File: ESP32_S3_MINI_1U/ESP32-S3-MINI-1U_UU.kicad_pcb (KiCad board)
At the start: 2 copper layers, 20.3 x 38.1 mm, 39 parts, among them IC1 TPS6282533DMQR, J1 Castellated_1x07, J2 USB4120-03-C, J3 Qwiic_Vertical, J4 Castellated_1x01, J5 Castellated_1x13, J6 Castellated_1x15, U1 ESP32-S3-MINI-1U, U2 LM66100DCK, U3 LM66100DCK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

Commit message: Sync Update
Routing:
- net IO3: track 6.08 -> 7.15 mm
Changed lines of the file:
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@@
-	)
-	(segment
-		(start 179.2 131.04)
-		(end 178.788768 130.628768)
-		(width 0.15)
-		(layer "F.Cu")
-		(net 7)
 	)
 	(segment
@@
 	)
 	(via
-		(at 178.76 130.7)
+		(at 179.2 131.04)
 		(size 0.5)
 		(drill 0.3)
@@
 	)
 	(segment
-		(start 178.831232 130.628768)
-		(end 178.76 130.557536)
+		(start 179.2 131.04)
+		(end 179.2 129.736388)
 		(width 0.15)
 		(layer "B.Cu")
@@
 	)
 	(segment
+		(start 179.2 129.736388)
+		(end 178.209 128.745388)
+		(width 0.15)
+		(layer "B.Cu")
+		(net 7)
+	)
+	(segment
 		(start 178.209 121.359)
-		(end 178.209 128.745388)
+		(end 175.95 119.1)
 		(width 0.15)
 		(layer "B.Cu")
@@
 	(segment
 		(start 178.209 128.745388)
-		(end 178.76 129.296388)
+		(end 178.209 121.359)
 		(width 0.15)
 		(layer "B.Cu")
@@
 	)
 	(segment
-		(start 178.76 129.296388)
-		(end 178.76 130.7)
-		(width 0.15)
-		(layer "B.Cu")
-		(net 7)
-	)
-	(segment
 		(start 175.95 119.1)
-		(end 178.209 121.359)
-		(width 0.15)
-		(layer "B.Cu")
-		(net 7)
-	)
-	(segment
-		(start 178.788768 130.628768)
-		(end 178.831232 130.628768)
-		(width 0.15)
-		(layer "B.Cu")
-		(net 7)
-	)
-	(segment
-		(start 174.651299 119.1)
-		(end 175.95 119.1)
+		(end 174.651299 119.1)
 		(width 0.15)
 		(layer "B.Cu")
@@
 	)
 	(segment
+		(start 172.316 124.364)
+		(end 172.316 124.44)
+		(width 0.15)
+		(layer "F.Cu")
+		(net 38)
+	)
+	(segment
+		(start 173.4 122.8)
+		(end 173.4 121.4)
+		(width 0.15)
+		(layer "F.Cu")
+		(net 38)
+	)
+	(segment
+		(start 174.85 119.95)
+		(end 175.4 119.95)
+		(width 0.15)
+		(layer "F.Cu")
+		(net 38)
+	)
+	(segment
+		(start 172.68 124)
+		(end 172.316 124.364)
+		(width 0.15)
+		(layer "F.Cu")
+		(net 38)
+	)
+	(segment
 		(start 172.316 123.884)
 		(end 172.316 124.43)
@@
 	)
 	(segment
-		(start 173.4 122.8)
-		(end 172.316 123.884)
+		(start 172.98 123.7)
+		(end 172.98 123.22)
 		(width 0.15)
 		(layer "F.Cu")
@@
 	)
 	(segment
-		(start 175.4 119.95)
+		(start 172.98 123.22)
+		(end 173.4 122.8)
+		(width 0.15)
+		(layer "F.Cu")
+		(net 38)
+	)
+	(segment
+		(start 173.4 121.4)
 		(end 174.85 119.95)
 		(width 0.15)
@@
 	)
 	(segment
-		(start 174.85 119.95)
-		(end 173.4 121.4)
-		(width 0.15)
-		(layer "F.Cu")
-		(net 38)
-	)
-	(segment
-		(start 173.4 121.4)
-		(end 173.4 122.8)
+		(start 172.316 124.364)
+		(end 172.98 123.7)
 		(width 0.15)
 		(layer "F.Cu")
@@
 	)
 	(via
-		(at 174.349914 131.989914)
+		(at 174.349914 132)
 		(size 0.5)
 		(drill 0.3)

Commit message: Trace cleanup
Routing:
- net GND: track 55.2 -> 63.0 mm
- net IO3: track 7.15 -> 6.09 mm
- added copper zone on F.Cu, net Net-(IC1-SW)
- added copper zone on F.Cu, net VSYS

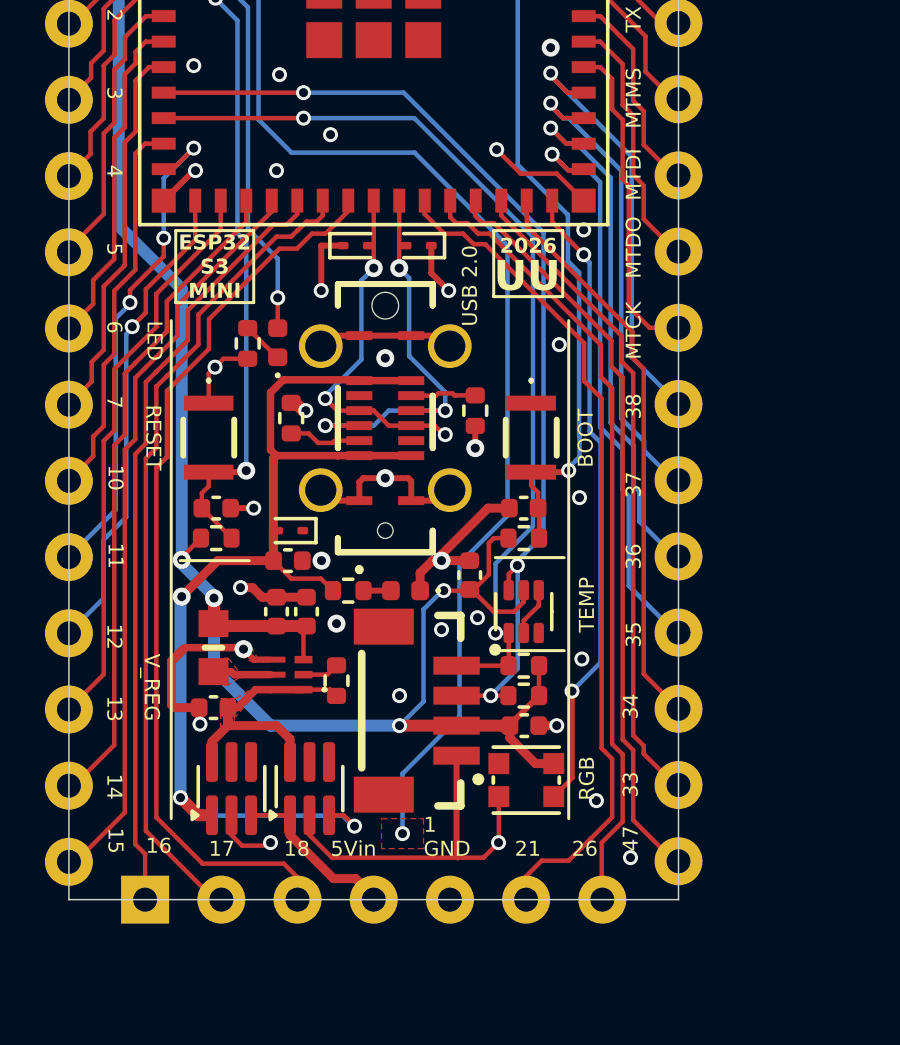
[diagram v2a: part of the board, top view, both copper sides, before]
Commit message: Differential USB routing
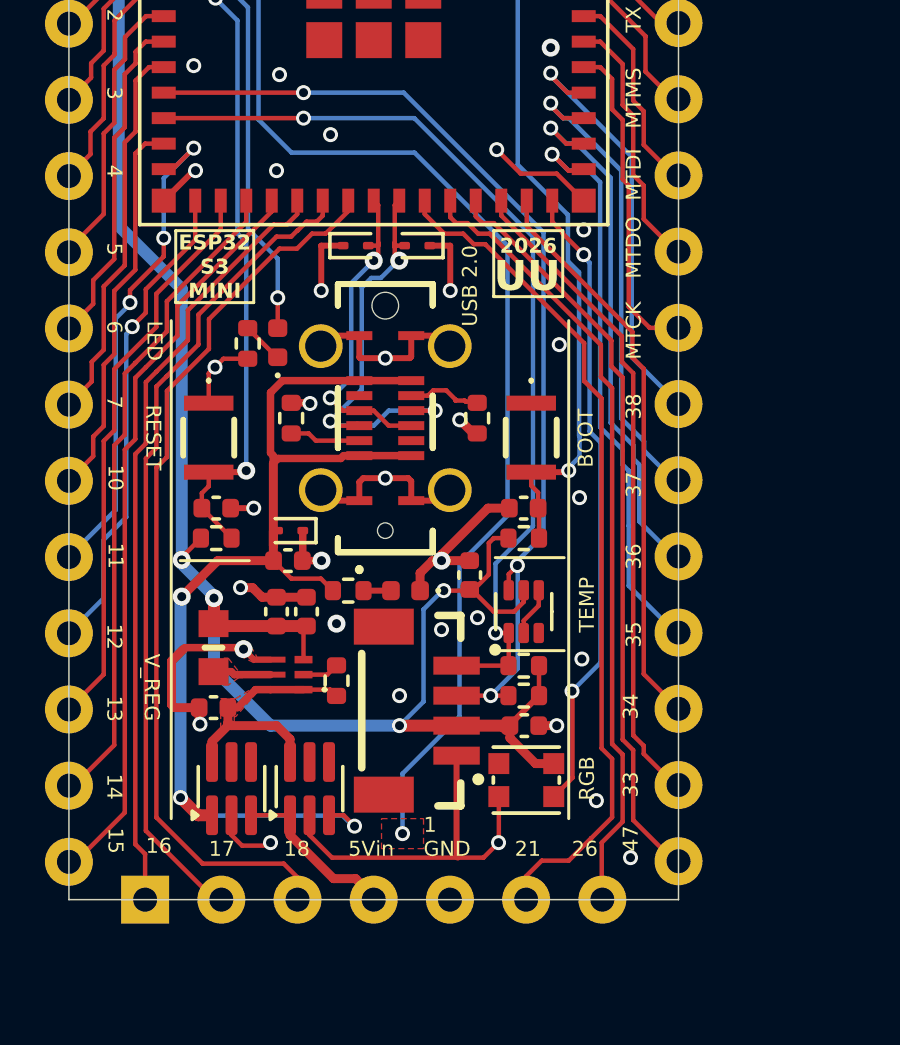
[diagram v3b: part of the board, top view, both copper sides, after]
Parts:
- moved R4 0.26 mm to (185.8, 135.1)
- moved D7 0.05 mm to (183.8, 129.3)
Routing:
- net GND: track 63.0 -> 66.6 mm
- net D-: track 11.7 -> 10.8 mm, vias 3 -> 2
- net D+: track 14.3 -> 14.8 mm

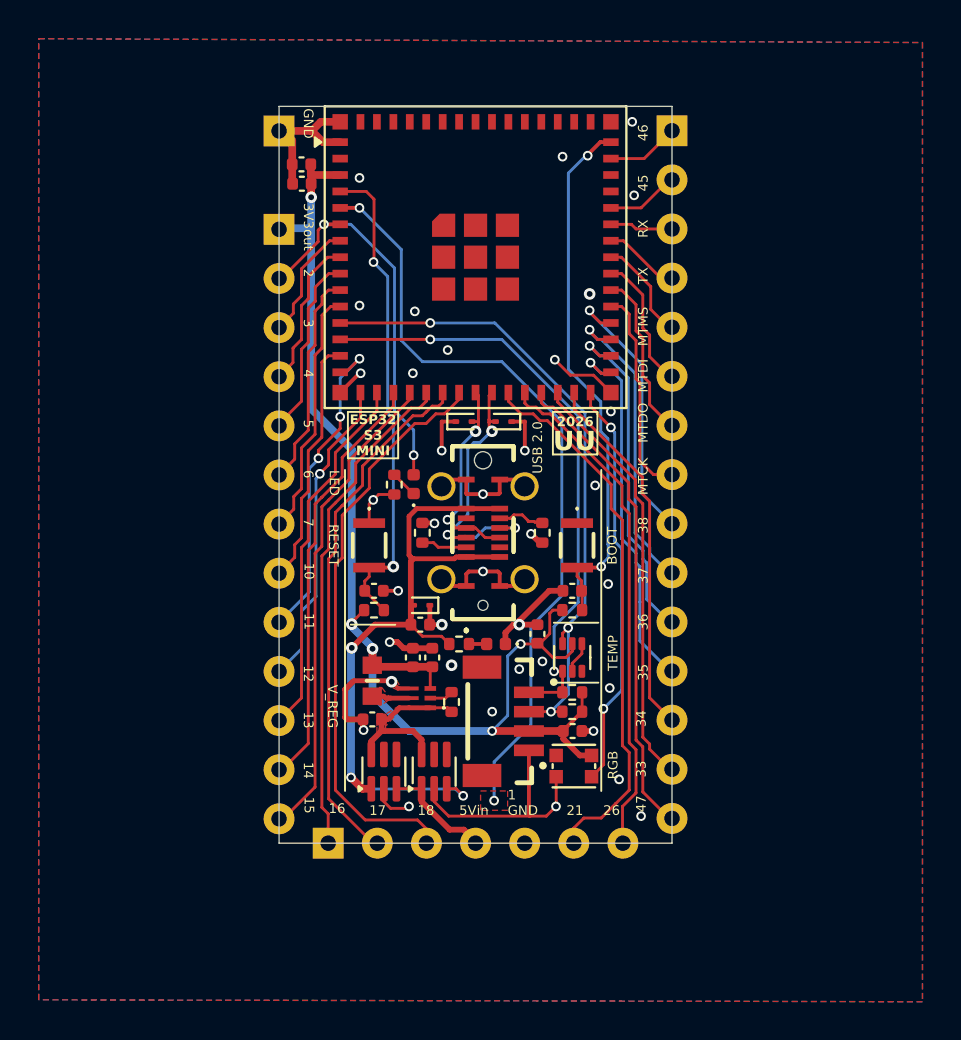
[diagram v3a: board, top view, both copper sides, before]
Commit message: Update ESP32 PCB projects and generated assets
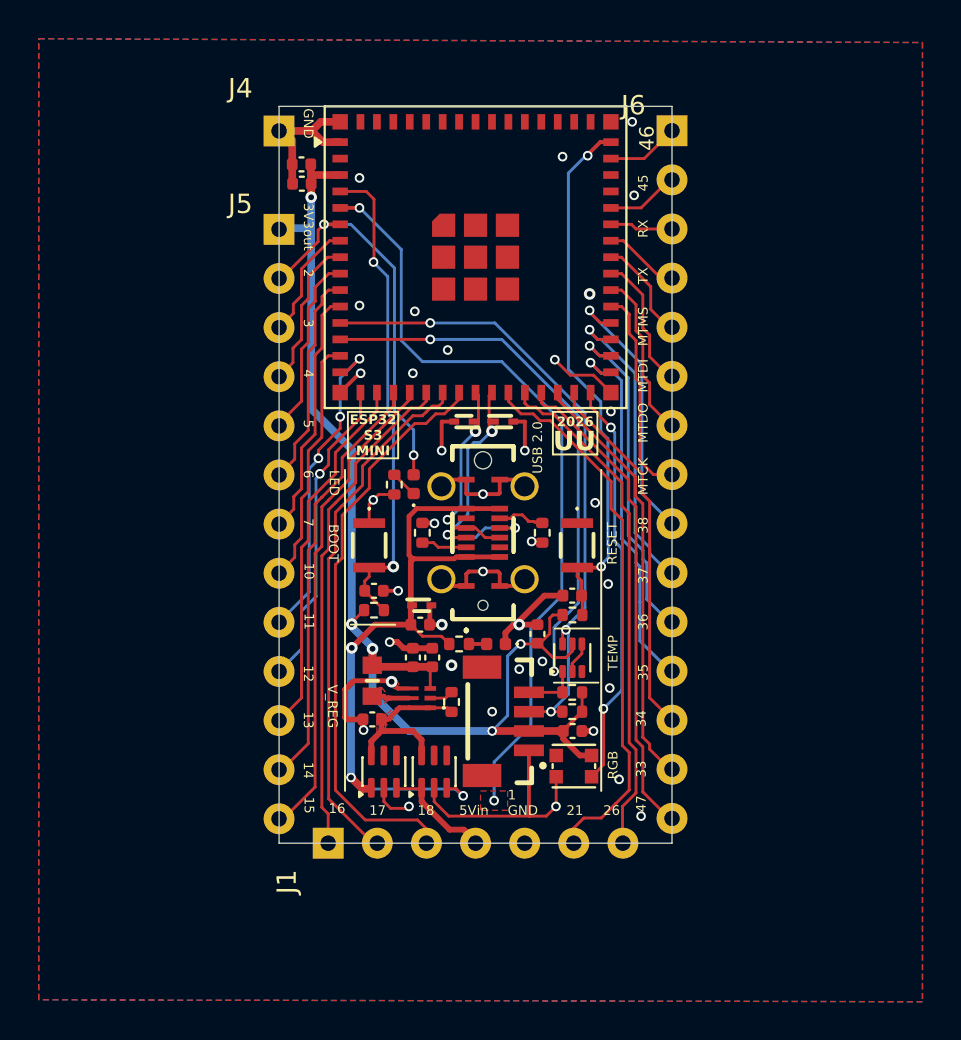
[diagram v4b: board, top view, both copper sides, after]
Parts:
- D1, D7, D8: footprint Diode_SMD:D_SOD-923 -> ESP32-S3-MINI-1U_Components:SODFL1006X40N
- IC1: footprint ESP32:TPS6282533DMQR -> ESP32-S3-MINI-1U_Components:TPS6282533DMQR
- J1: footprint Castellated:Castellated_1x07_P2.54mm_D0.80mm -> Castellated_Connectors:Castellated_1x07_P2.54mm_D0.80mm
- J2: footprint ESP32:USB412003C -> ESP32-S3-MINI-1U_Components:USB412003C
- J4: footprint Castellated:Castellated_1x01_P2.54mm_D0.80mm -> Castellated_Connectors:Castellated_1x01_P2.54mm_D0.80mm
- J5: footprint Castellated:Castellated_1x13_P2.54mm_D0.80mm -> Castellated_Connectors:Castellated_1x13_P2.54mm_D0.80mm
- J6: footprint Castellated:Castellated_1x15_P2.54mm_D0.80mm -> Castellated_Connectors:Castellated_1x15_P2.54mm_D0.80mm
- L1: footprint ESP32:INDC1608X75N -> ESP32-S3-MINI-1U_Components:INDC1608X75N
- S1, S2: footprint ESP32:NANOT160AS -> ESP32-S3-MINI-1U_Components:NANOT160AS
- U4: value TMP102 -> TMP112xxDRL; footprint PCM_SparkFun-Semiconductor-Standard:SOT-563 -> Package_TO_SOT_SMD:SOT-563
- moved R17 0.25 mm to (187.4, 139.3)
- moved C12 0.25 mm to (187.4, 138.3)
- turned D1 to 0 degrees
- turned D7 to 0 degrees
- turned D8 to 180 degrees
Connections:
- D1 pad 1: GND -> V_USB
- D1 pad 2: V_USB -> GND
- D7 pad 1: GND -> D+
- D7 pad 2: D+ -> GND
- D8 pad 1: GND -> D-
- D8 pad 2: D- -> GND
